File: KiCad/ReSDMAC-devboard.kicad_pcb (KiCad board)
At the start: 4 copper layers, 91.2 x 52 mm, 9 parts, among them J1 USB_B_Micro, J2 Conn_02x01, J3 Conn_01x01, U1 PLCC-84-Plug, U2 Super_DMAC_SMD_socket, U3 Super_DMAC_TH_socket

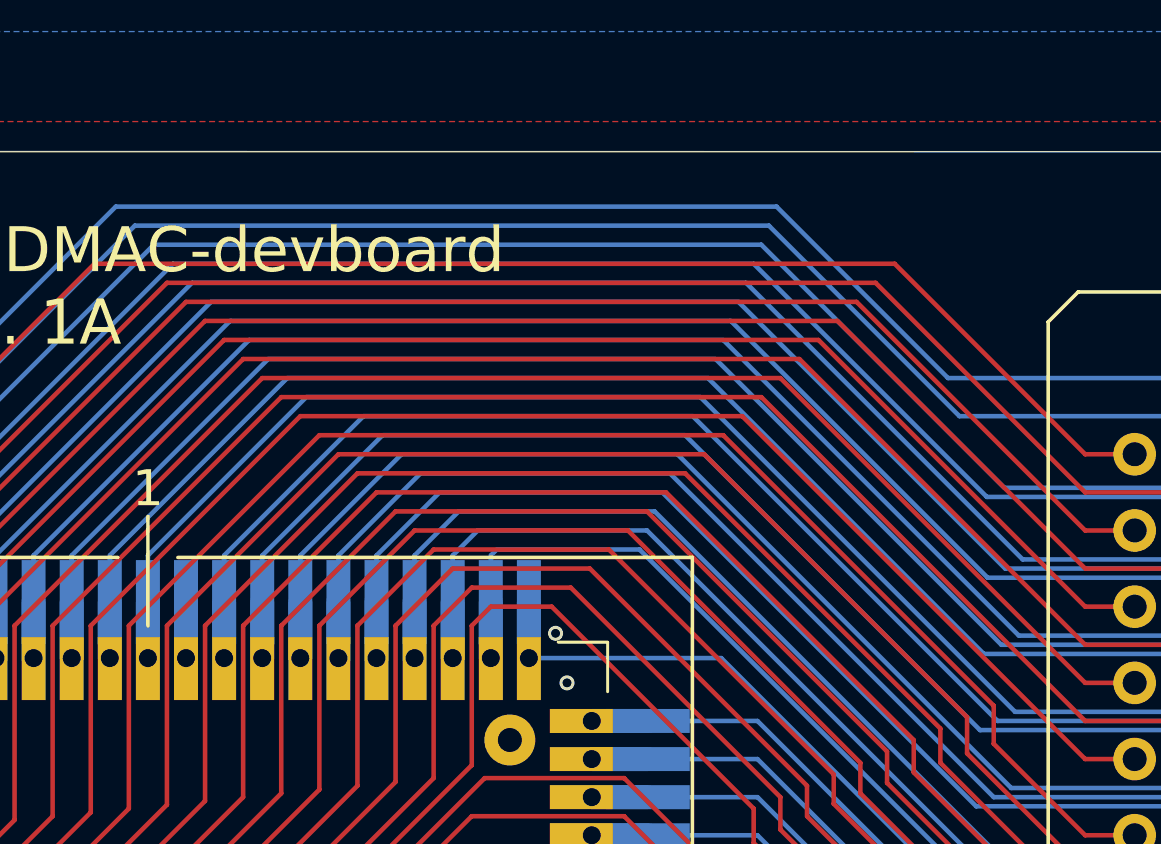
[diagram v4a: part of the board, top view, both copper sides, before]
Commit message: small routing fix, only cosmetic
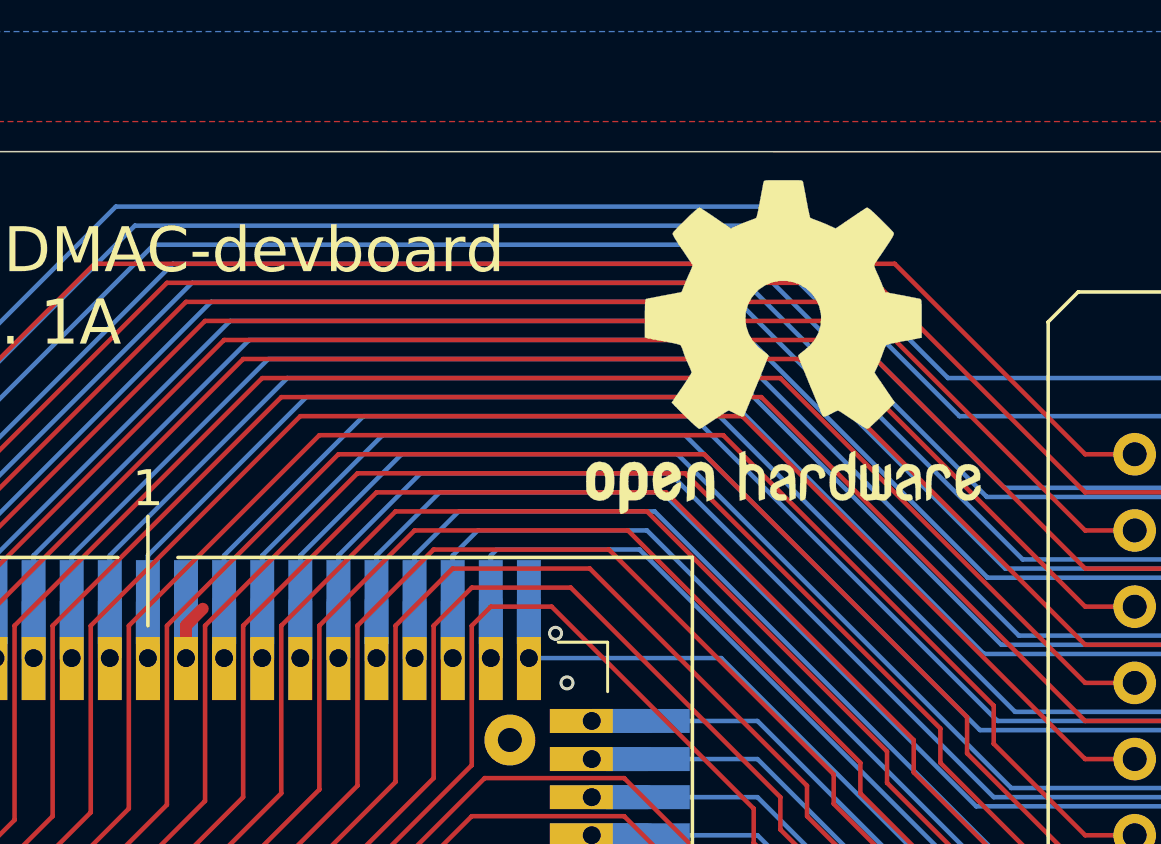
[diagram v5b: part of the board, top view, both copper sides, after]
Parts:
- added REF**: OSHW-Logo2_14.6x12mm_SilkScreen, Symbol:OSHW-Logo2_14.6x12mm_SilkScreen, F.Cu at (158.8, 91.1)
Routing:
- net GND: track 8.38 -> 10.3 mm
